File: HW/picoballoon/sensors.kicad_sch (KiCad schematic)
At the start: 9 parts, among them IC1 HIH7130-021-001, U2 MPL3115A2, U4 MCP9802

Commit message: aprs test board
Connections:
- net SCL: no longer U4.4 (SCLK)
- net SDA: no longer U4.5 (SDA)
- new net SCL_TEMP: U4.4 (SCLK)
- new net SDA_TEMP: U4.5 (SDA)
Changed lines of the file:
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@@
+	(wire
+		(pts
+			(xy 151.13 181.61) (xy 161.29 181.61)
+		)
+		(stroke
+			(width 0)
+			(type default)
+		)
+	)
 	(wire
 		(pts
@@
 	(wire
 		(pts
-			(xy 45.72 49.53) (xy 50.8 49.53)
-		)
-		(stroke
-			(width 0)
-			(type default)
-		)
-	)
-	(wire
-		(pts
-			(xy 45.72 52.07) (xy 50.8 52.07)
+			(xy 40.64 49.53) (xy 50.8 49.53)
+		)
+		(stroke
+			(width 0)
+			(type default)
+		)
+	)
+	(wire
+		(pts
+			(xy 40.64 52.07) (xy 50.8 52.07)
 		)
 		(stroke
@@
 	(wire
 		(pts
-			(xy 154.94 179.07) (xy 161.29 179.07)
+			(xy 151.13 175.26) (xy 161.29 175.26)
 		)
 		(stroke
@@
 	(wire
 		(pts
-			(xy 154.94 181.61) (xy 161.29 181.61)
+			(xy 151.13 177.8) (xy 161.29 177.8)
 		)
 		(stroke
@@
 		(pts
 			(xy 97.79 139.7) (xy 97.79 146.05)
+		)
+		(stroke
+			(width 0)
+			(type default)
+		)
+	)
+	(wire
+		(pts
+			(xy 151.13 184.15) (xy 161.29 184.15)
 		)
 		(stroke
@@
 		)
 	)
-	(label "SDA"
-		(at 45.72 49.53 0)
-		(fields_autoplaced yes)
-		(effects
-			(font
-				(size 1.27 1.27)
-			)
-			(justify left bottom)
-		)
-	)
-	(label "SDA"
-		(at 154.94 179.07 0)
-		(fields_autoplaced yes)
-		(effects
-			(font
-				(size 1.27 1.27)
-			)
-			(justify left bottom)
-		)
-	)
 	(label "SCL"
-		(at 154.94 181.61 0)
-		(fields_autoplaced yes)
-		(effects
-			(font
-				(size 1.27 1.27)
-			)
-			(justify left bottom)
-		)
-	)
-	(label "SCL"
-		(at 45.72 52.07 0)
+		(at 151.13 184.15 0)
+		(fields_autoplaced yes)
+		(effects
+			(font
+				(size 1.27 1.27)
+			)
+			(justify left bottom)
+		)
+	)
+	(label "SDA_TEMP"
+		(at 40.64 49.53 0)
+		(fields_autoplaced yes)
+		(effects
+			(font
+				(size 1.27 1.27)
+			)
+			(justify left bottom)
+		)
+	)
+	(label "SDA_TEMP"
+		(at 151.13 175.26 0)
+		(fields_autoplaced yes)
+		(effects
+			(font
+				(size 1.27 1.27)
+			)
+			(justify left bottom)
+		)
+	)
+	(label "SCL_TEMP"
+		(at 151.13 177.8 0)
+		(fields_autoplaced yes)
+		(effects
+			(font
+				(size 1.27 1.27)
+			)
+			(justify left bottom)
+		)
+	)
+	(label "SCL_TEMP"
+		(at 40.64 52.07 0)
 		(fields_autoplaced yes)
 		(effects
@@
 	)
 	(label "SDA"
+		(at 151.13 181.61 0)
+		(fields_autoplaced yes)
+		(effects
+			(font
+				(size 1.27 1.27)
+			)
+			(justify left bottom)
+		)
+	)
+	(label "SDA"
 		(at 190.5 52.07 0)
 		(fields_autoplaced yes)
@@
 		)
 	)
+	(hierarchical_label "SDA_TEMP"
+		(shape bidirectional)
+		(at 161.29 175.26 0)
+		(fields_autoplaced yes)
+		(effects
+			(font
+				(size 1.27 1.27)
+			)
+			(justify left)
+		)
+	)
 	(hierarchical_label "SDA"
 		(shape bidirectional)
-		(at 161.29 179.07 0)
+		(at 161.29 181.61 0)
+		(fields_autoplaced yes)
+		(effects
+			(font
+				(size 1.27 1.27)
+			)
+			(justify left)
+		)
+	)
+	(hierarchical_label "SCL_TEMP"
+		(shape input)
+		(at 161.29 177.8 0)
 		(fields_autoplaced yes)
 		(effects
@@
 	(hierarchical_label "SCL"
 		(shape input)
-		(at 161.29 181.61 0)
-		(fields_autoplaced yes)
-		(effects
+		(at 161.29 184.15 0)
+		(fields_autoplaced yes)
+		(effects

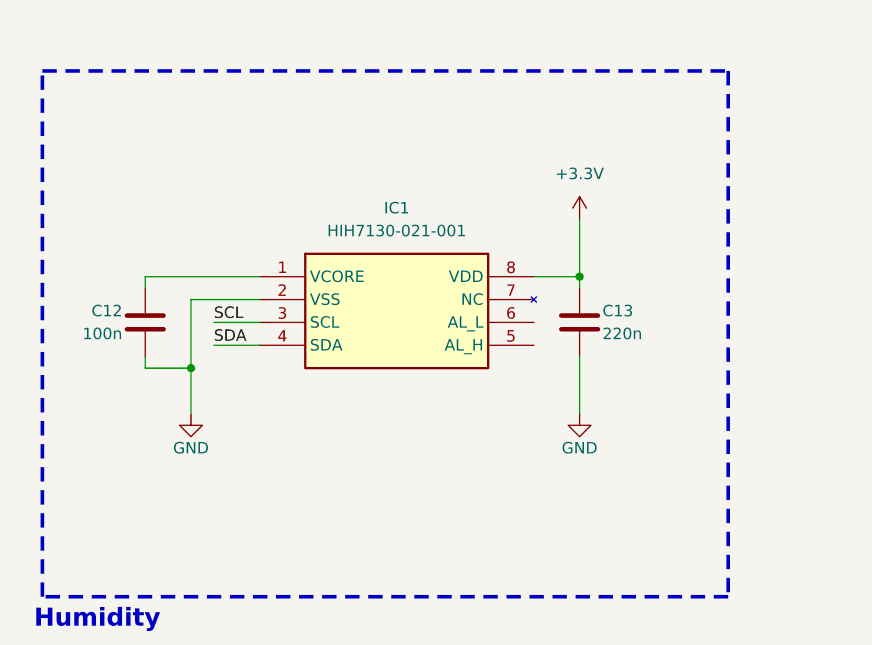
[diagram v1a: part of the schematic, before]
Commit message: some devices replaced
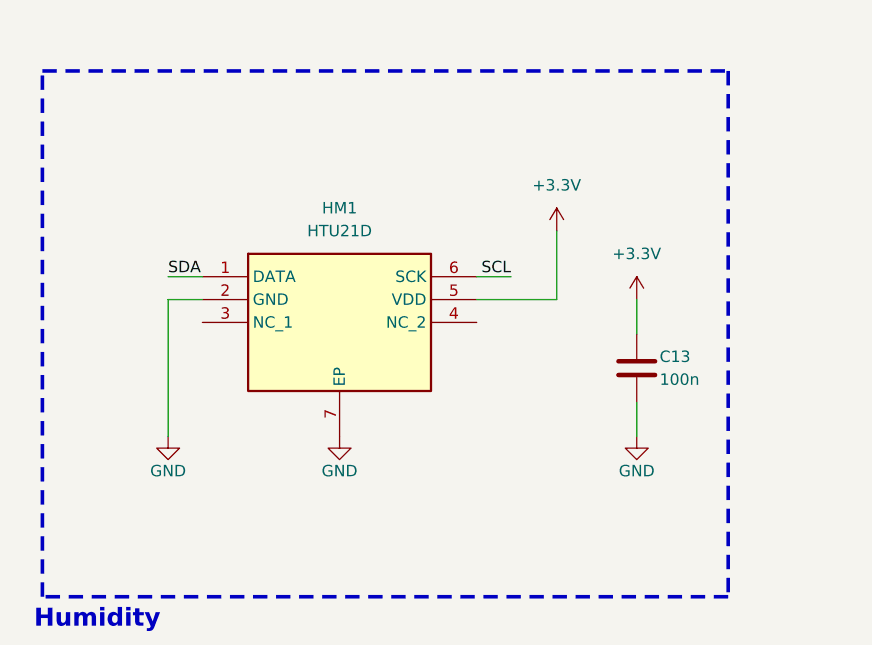
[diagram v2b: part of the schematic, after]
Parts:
- removed C12: 100n, symbol Device:C
- removed IC1: HIH7130-021-001, SOIC-8_SMD_1, symbol Library:HIH7130-021-001
- added HM1: HTU21D, SON100P300X300X100-7N-D, symbol Library:HTU21D
- C13: value 220n -> 100n
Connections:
- net +3.3V: now also HM1.5 (VDD)
- net GND: now also HM1.2 (GND), HM1.7 (EP)
- net SCL: now also HM1.6 (SCK)
- net SDA: now also HM1.1 (DATA)
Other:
- moved on the sheet: C13

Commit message: pcb
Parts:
- C1, C13, C2, C3, C6: footprint (none) -> Capacitor_SMD:C_0603_1608Metric_Pad1.08x0.95mm_HandSolder
- HM1: footprint SON100P300X300X100-7N-D -> Library:SON100P300X300X100-7N-D
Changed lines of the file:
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@@
 			)
 		)
-		(property "Footprint" ""
+		(property "Footprint" "Capacitor_SMD:C_0603_1608Metric_Pad1.08x0.95mm_HandSolder"
 			(at 205.4352 100.33 0)
 			(effects
@@
 			)
 		)
-		(property "Footprint" ""
+		(property "Footprint" "Capacitor_SMD:C_0603_1608Metric_Pad1.08x0.95mm_HandSolder"
 			(at 218.1352 100.33 0)
 			(effects
@@
 			)
 		)
-		(property "Footprint" ""
+		(property "Footprint" "Capacitor_SMD:C_0603_1608Metric_Pad1.08x0.95mm_HandSolder"
 			(at 105.1052 160.02 0)
 			(effects
@@
 			)
 		)
-		(property "Footprint" ""
+		(property "Footprint" "Capacitor_SMD:C_0603_1608Metric_Pad1.08x0.95mm_HandSolder"
 			(at 89.8652 50.8 0)
 			(effects
@@
 			)
 		)
-		(property "Footprint" "SON100P300X300X100-7N-D"
+		(property "Footprint" "Library:SON100P300X300X100-7N-D"
 			(at 82.55 240.97 0)
 			(effects
@@
 			)
 		)
-		(property "Footprint" ""
+		(property "Footprint" "Capacitor_SMD:C_0603_1608Metric_Pad1.08x0.95mm_HandSolder"
 			(at 229.5652 68.58 0)
 			(effects

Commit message: test points
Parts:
- renumbered C6 to C19, C2 to C20, C1 to C21, C3 to C22, C13 to C23
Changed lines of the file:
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@@
 		(on_board yes)
 		(dnp no)
-		(property "Reference" "C1"
+		(property "Reference" "C21"
 			(at 207.01 95.25 0)
 			(effects
@@
 			(project ""
 				(path "/f2ac4b1c-d093-4228-80b2-7ee26b75b20f/46223dc2-f263-43b3-a11d-43066bfcef5c"
-					(reference "C1")
+					(reference "C21")
 					(unit 1)
 				)
@@
 		(on_board yes)
 		(dnp no)
-		(property "Reference" "C3"
+		(property "Reference" "C22"
 			(at 219.71 95.25 0)
 			(effects
@@
 			(project "picoballoon"
 				(path "/f2ac4b1c-d093-4228-80b2-7ee26b75b20f/46223dc2-f263-43b3-a11d-43066bfcef5c"
-					(reference "C3")
+					(reference "C22")
 					(unit 1)
 				)
@@
 		(on_board yes)
 		(dnp no)
-		(property "Reference" "C13"
+		(property "Reference" "C23"
 			(at 106.68 154.94 0)
 			(effects
@@
 			(project "picoballoon"
 				(path "/f2ac4b1c-d093-4228-80b2-7ee26b75b20f/46223dc2-f263-43b3-a11d-43066bfcef5c"
-					(reference "C13")
+					(reference "C23")
 					(unit 1)
 				)
@@
 		(on_board yes)
 		(dnp no)
-		(property "Reference" "C6"
+		(property "Reference" "C19"
 			(at 91.44 45.72 0)
 			(effects
@@
 			(project "picoballoon"
 				(path "/f2ac4b1c-d093-4228-80b2-7ee26b75b20f/46223dc2-f263-43b3-a11d-43066bfcef5c"
-					(reference "C6")
+					(reference "C19")
 					(unit 1)
 				)
@@
 		(on_board yes)
 		(dnp no)
-		(property "Reference" "C2"
+		(property "Reference" "C20"
 			(at 231.14 63.5 0)
 			(effects
@@
 			(project "picoballoon"
 				(path "/f2ac4b1c-d093-4228-80b2-7ee26b75b20f/46223dc2-f263-43b3-a11d-43066bfcef5c"
-					(reference "C2")
-					(unit 1)
-				)
+					(reference "C20")
+					(unit 1)
+				)

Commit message: APRS testing with Arduinno
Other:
- company: (none) -> Vojtech Piroch
- title: (none) -> Sensors
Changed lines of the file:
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@@
 	(generator_version "8.0")
 	(paper "A4")
+	(title_block
+		(title "Sensors")
+		(date "2025-01-03")
+		(company "Vojtech Piroch")
+	)
 	(junction
 		(at 204.47 91.44)
